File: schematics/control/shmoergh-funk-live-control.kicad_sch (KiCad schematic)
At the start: 6 parts

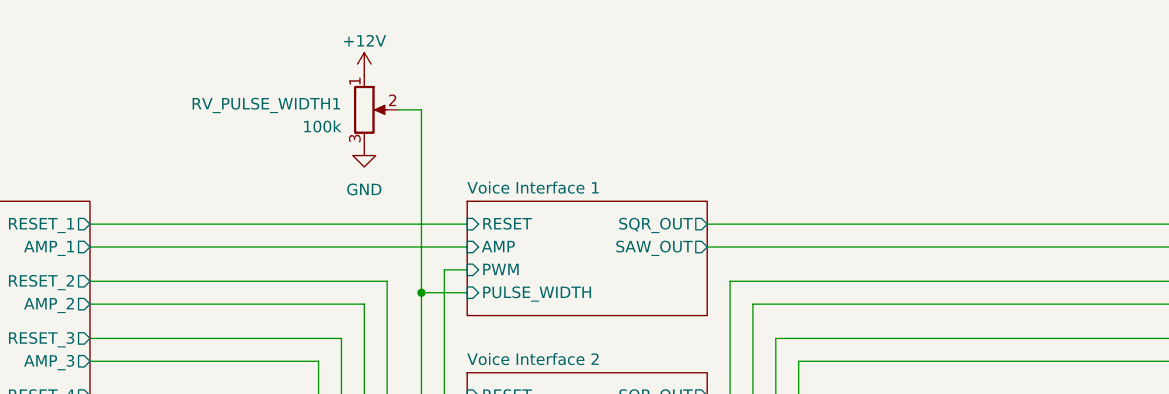
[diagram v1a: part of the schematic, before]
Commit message: DCO schematic update
Changed the DCO design from using a PNP transistor for the switch,
positive charge and an inverting amp with bias for the saw output. This
allows to bias the sawtooth output to oscillate around 0V which makes
possible to set precise pulse width values for all voices regardless of
potential component differences. Also, this eventually needs less
component altogether.
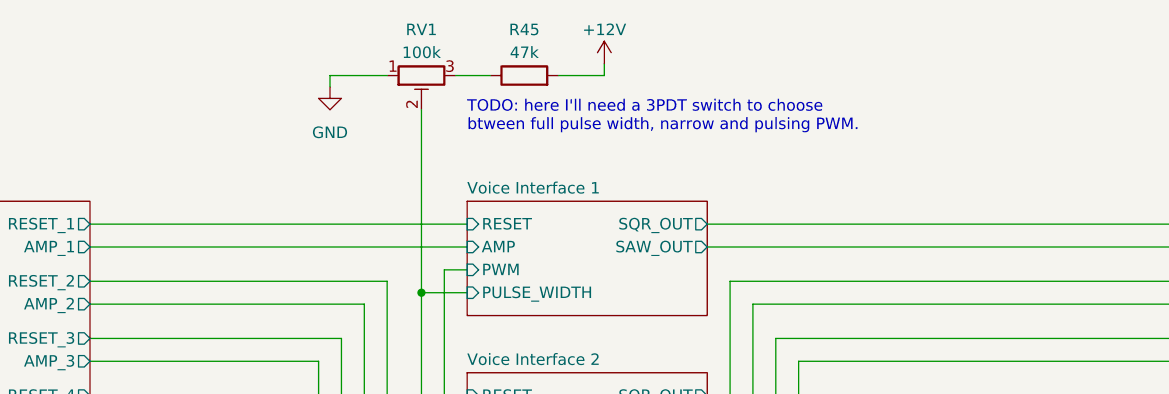
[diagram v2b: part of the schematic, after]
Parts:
- removed RV_PULSE_WIDTH1: 100k, Shmoergh_Custom_Footprints:NSL25_01x03_Vertical, symbol Device:R_Potentiometer
- added R45: 47k, symbol Device:R
- added RV1: 100k, symbol Device:R_Potentiometer_Trim
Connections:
- net +12V: now also R45.2
- net GND: now also RV1.1
- net Voice Interface 1/PULSE_WIDTH: now also RV1.2
- new net: R45.1, RV1.3
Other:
- note added: "TODO: here I'll need a 3PDT switch to choose btween full pulse width, narrow and pulsing PWM."

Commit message: Added pulse width mod schematics
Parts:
- removed R45: 47k, symbol Device:R
- removed RV1: 100k, symbol Device:R_Potentiometer_Trim
- renumbered H5 to H4, H6 to H5
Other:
- sheet LFO renamed LFO + PWM
- sheet LFO + PWM ports: added PULSE_WIDTH; removed none
- note removed: "TODO: here I'll need a 3PDT switch to choose btween full pulse width, narrow and pulsing PWM."

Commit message: Updated VCA
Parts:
- added JP_INTERNAL_VCA_GATE1, JP_INTERNAL_VCA_IN1, JP_INTERNAL_VCA_OUT1: jmpr, symbol Jumper:Jumper_2_Open
- added J_EXTERNAL_VCA1: Conn_01x03, symbol Connector_Generic:Conn_01x03
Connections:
- net Digital/ENVELOPE: now also JP_INTERNAL_VCA_GATE1.2 (B), J_EXTERNAL_VCA1.2 (Pin_2)
- net Filter Interface/AUDIO_OUT: now also JP_INTERNAL_VCA_IN1.2 (B)
- net Output/AUDIO_IN: now also JP_INTERNAL_VCA_OUT1.2 (B), J_EXTERNAL_VCA1.3 (Pin_3)
- new net VCA (Internal)/AUDIO_IN: JP_INTERNAL_VCA_IN1.1 (A), J_EXTERNAL_VCA1.1 (Pin_1)
- new net VCA (Internal)/AUDIO_OUT: JP_INTERNAL_VCA_OUT1.1 (A)
- new net VCA (Internal)/GATE: JP_INTERNAL_VCA_GATE1.1 (A)
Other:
- sheet VCA (discrete) renamed VCA (Internal)
- sheet Digital ports: added FILTER_MOD; removed none
- sheet Filter Interface ports: added FILTER_DIGITAL_MOD; removed none
- note added: "Escape valve for external VCA if needed"
